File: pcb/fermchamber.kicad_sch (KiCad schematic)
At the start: 24 parts, among them J1 12V IN, J2 DALLAS SENSOR, J3 5V OUT, J4 230 IN, J7 BME280 SENSOR, U1 ESP32-S2-DevKitM, U2 LM2575-5.0BT

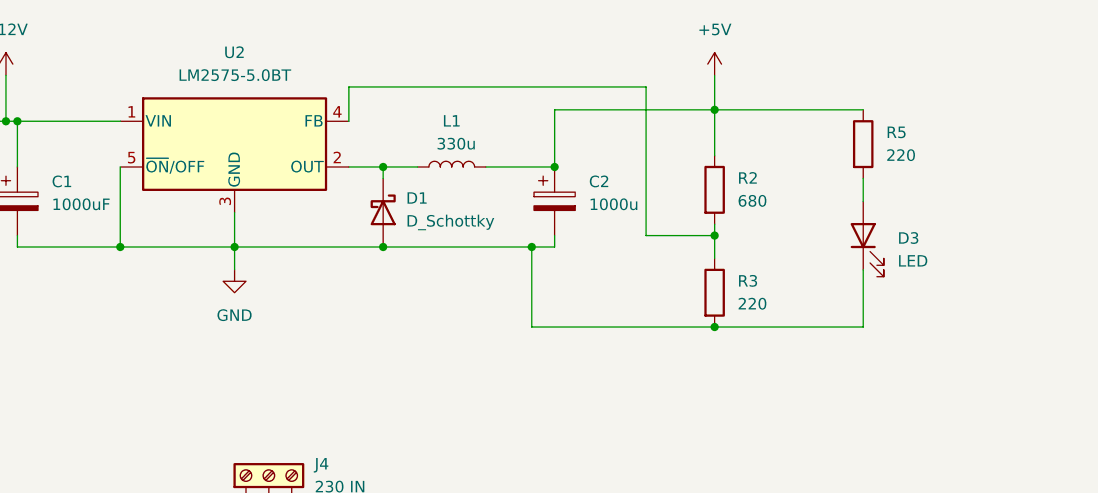
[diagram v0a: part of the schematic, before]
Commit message: fixed capactior, inductor and, voltage ic footprint in schematic; added missing labels on the pcb; clarified and added missing items in the BOM
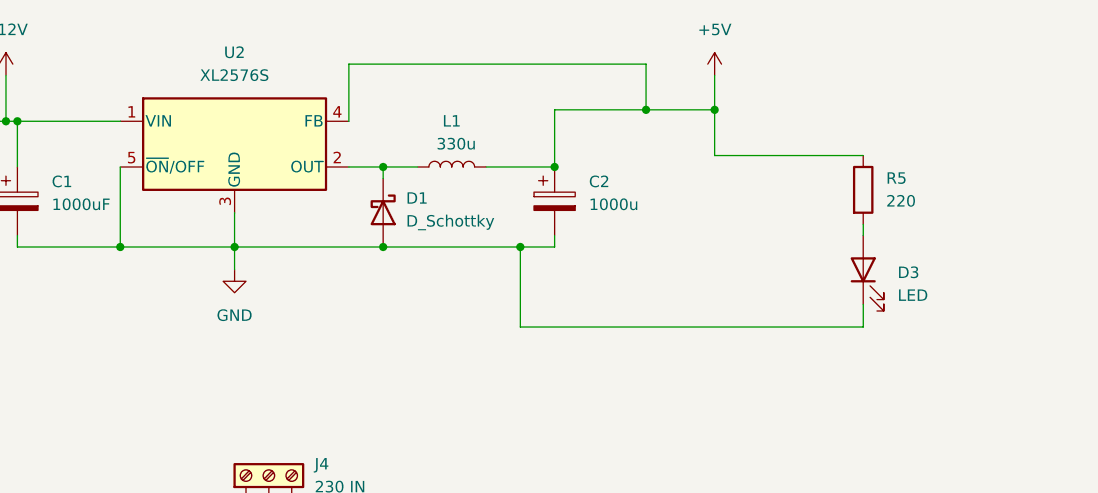
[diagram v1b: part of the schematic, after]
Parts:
- removed R2: 680, Resistor_THT:R_Axial_DIN0411_L9.9mm_D3.6mm_P12.70mm_Horizontal, symbol Device:R
- removed R3: 220, Resistor_THT:R_Axial_DIN0411_L9.9mm_D3.6mm_P12.70mm_Horizontal, symbol Device:R
- C1, C2, C3, C4, C5: footprint Capacitor_THT:CP_Radial_D8.0mm_P3.50mm -> Capacitor_THT:CP_Radial_D12.5mm_P5.00mm
- L1: footprint Inductor_THT:L_Axial_L16.0mm_D6.3mm_P20.32mm_Horizontal_Fastron_VHBCC -> Inductor_THT:L_Radial_D10.0mm_P5.00mm_Fastron_07P
- U2: value LM2575-5.0BT -> XL2576S
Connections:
- net +5V: now also U2.4 (FB)
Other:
- moved on the sheet: D3, R5

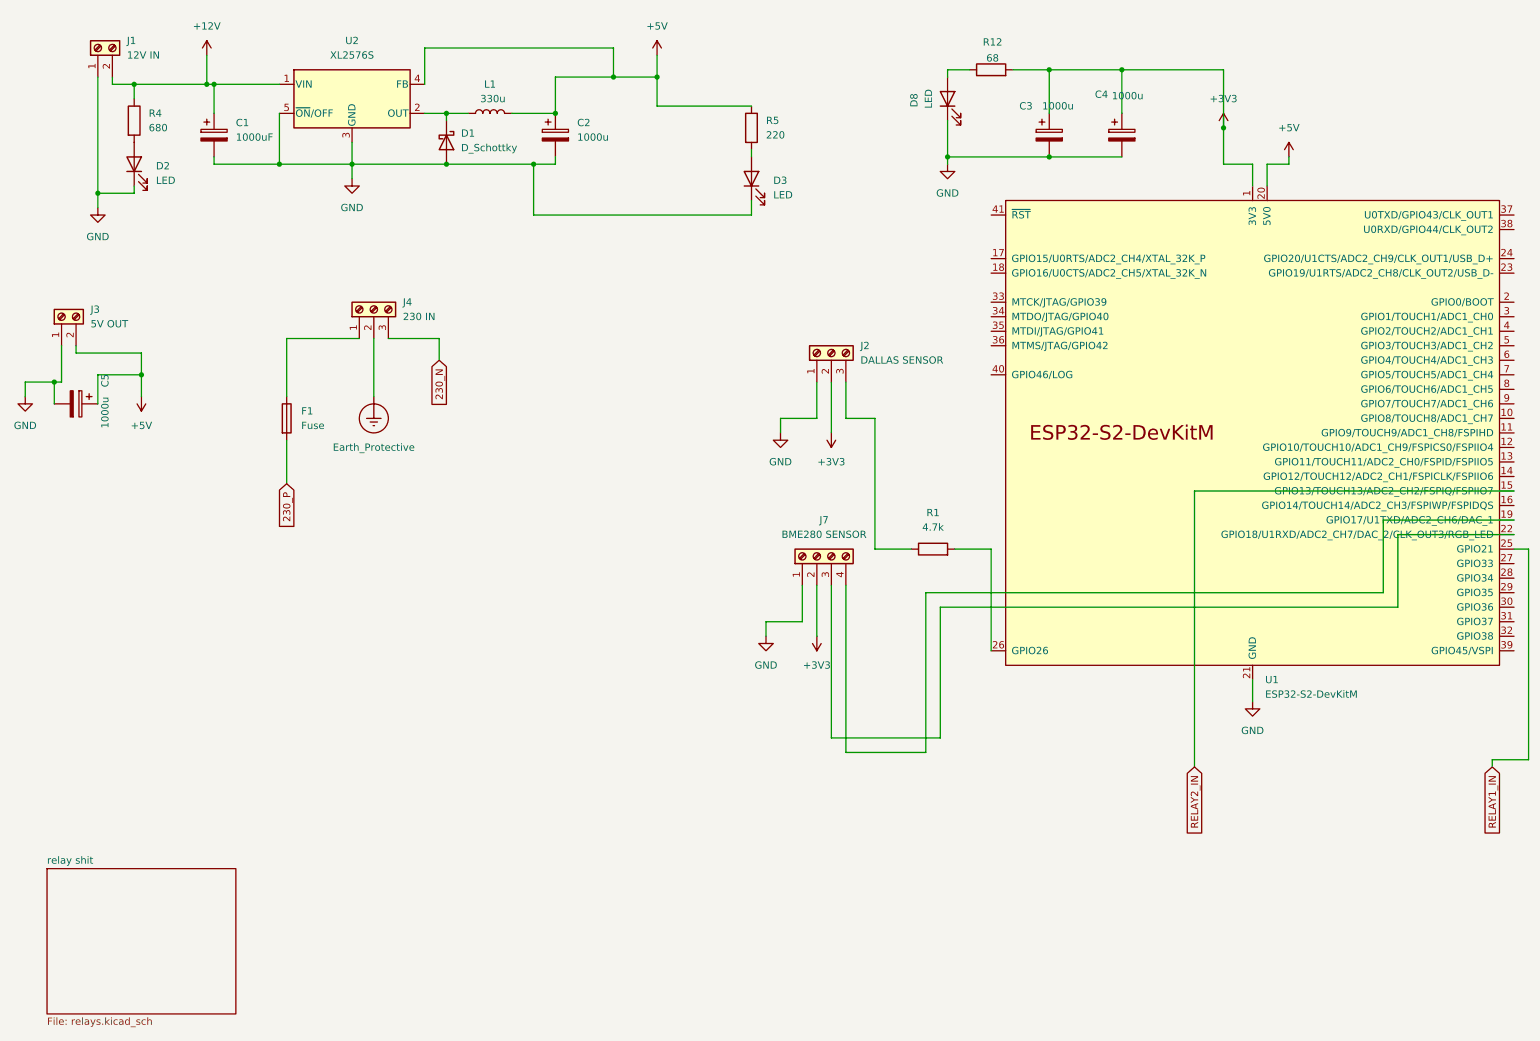
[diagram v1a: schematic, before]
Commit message: changed esp board to nodemcu 32s, limited current on leds, added diode for 5v usb programming backfeed, made switched labels more clear, fixed dallas data bus pull up, added pcb holes for mounting, removed unnecessary BOM items, removed relay optocoupler, re-routed pcb, fixed TODOs, added new render
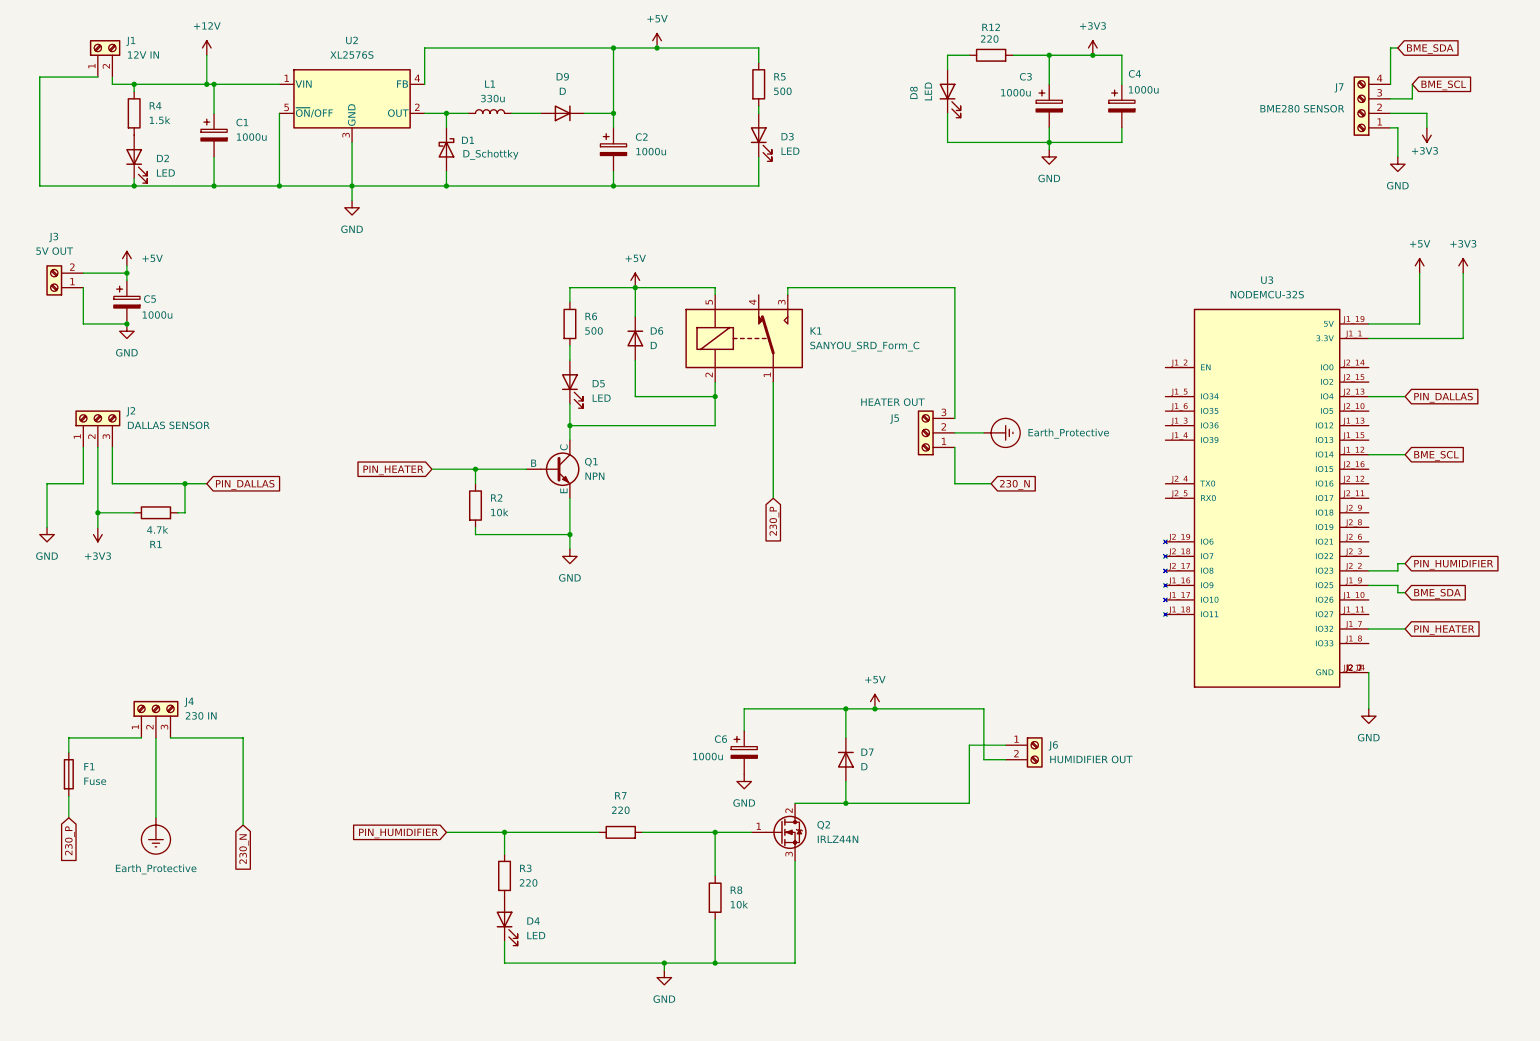
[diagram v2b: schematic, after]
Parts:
- removed U1: ESP32-S2-DevKitM, PCM_Espressif:ESP32-S2-DevKitM, symbol PCM_Espressif:ESP32-S2-DevKitM
- added C6: 1000u, Capacitor_THT:CP_Radial_D12.5mm_P5.00mm, symbol Device:C_Polarized
- added D4, D5: LED, LED_THT:LED_D3.0mm, symbol Device:LED
- added D6, D7, D9: D, Diode_THT:D_A-405_P7.62mm_Horizontal, symbol Device:D
- added J5: HEATER OUT, TerminalBlock_Phoenix:TerminalBlock_Phoenix_MKDS-1,5-3-5.08_1x03_P5.08mm_Horizontal, symbol Connector:Screw_Terminal_01x03
- added J6: HUMIDIFIER OUT, TerminalBlock_Phoenix:TerminalBlock_Phoenix_MKDS-1,5-2-5.08_1x02_P5.08mm_Horizontal, symbol Connector:Screw_Terminal_01x02
- added K1: SANYOU_SRD_Form_C, Relay_THT:Relay_SPDT_SANYOU_SRD_Series_Form_C, symbol Relay:SANYOU_SRD_Form_C
- added Q1: NPN, Package_TO_SOT_THT:TO-126-3_Vertical, symbol Simulation_SPICE:NPN
- added Q2: IRLZ44N, Package_TO_SOT_THT:TO-220-3_Vertical, symbol Transistor_FET:IRLZ44N
- added R2, R8: 10k, Resistor_THT:R_Axial_DIN0411_L9.9mm_D3.6mm_P12.70mm_Horizontal, symbol Device:R
- added R3, R7: 220, Resistor_THT:R_Axial_DIN0411_L9.9mm_D3.6mm_P12.70mm_Horizontal, symbol Device:R
- added R6: 500, Resistor_THT:R_Axial_DIN0411_L9.9mm_D3.6mm_P12.70mm_Horizontal, symbol Device:R
- added U3: NODEMCU-32S, NodeMcuFootprint:MODULE_NODEMCU-32S, symbol NODEMCU-32S:NODEMCU-32S
- C1: value 1000uF -> 1000u
- R12: value 68 -> 220
- R4: value 680 -> 1.5k
- R5: value 220 -> 500
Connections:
- net +3V3: now also R1.1, U3.J1_1 (3.3V)
- net +5V: now also C6.1, D6.1 (K), D7.1 (K), D9.1 (K), J6.2 (Pin_2), K1.5, R6.1, U3.J1_19 (5V); no longer L1.2
- net 230_N: now also J5.1 (Pin_1)
- net 230_P: now also K1.1
- net Earth_Protective: now also J5.2 (Pin_2)
- net GND: now also C6.2, D4.1 (K), Q1.3 (E), Q2.3 (S), R2.2, R8.2, U3.J1_14 (GND), U3.J2_1 (GND), U3.J2_7 (GND)
- net PIN_DALLAS: now reaches J2.3 (Pin_3)
- net PIN_DALLAS: now also R1.2, U3.J2_13 (IO4); no longer R1.1
- net BME_SCL: now reaches J7.3 (Pin_3)
- net BME_SCL: now also U3.J1_12 (IO14)
- net BME_SDA: now reaches J7.4 (Pin_4)
- net BME_SDA: now also U3.J1_9 (IO25)
- new net: D5.1 (K), D6.2 (A), K1.2, Q1.1 (C)
- new net: D5.2 (A), R6.2
- new net: D9.2 (A), L1.2
- new net: D7.2 (A), J6.1 (Pin_1), Q2.2 (D)
- new net: D4.2 (A), R3.2
- new net: Q2.1 (G), R7.2, R8.1
- new net: J5.3 (Pin_3), K1.3
- new net PIN_HEATER: Q1.2 (B), R2.1, U3.J1_7 (IO32)
- new net PIN_HUMIDIFIER: R3.1, R7.1, U3.J2_2 (IO23)
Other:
- removed sheet relay shit
- moved on the sheet: C2, C3, C4, C5, D1, D2, D3, D8, F1, J3, J4, R12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
